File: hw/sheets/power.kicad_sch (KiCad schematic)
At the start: 36 parts, among them U1 AP62600SJ-7, U2 AP62300WU-7, U3 MCP4661-104E_ST, U4 TPS22990DMLR, U5 AZ1117CH-3.3TRG1, U6 AZ1117CH-1.8TRG1, U7 AP62300WU-7

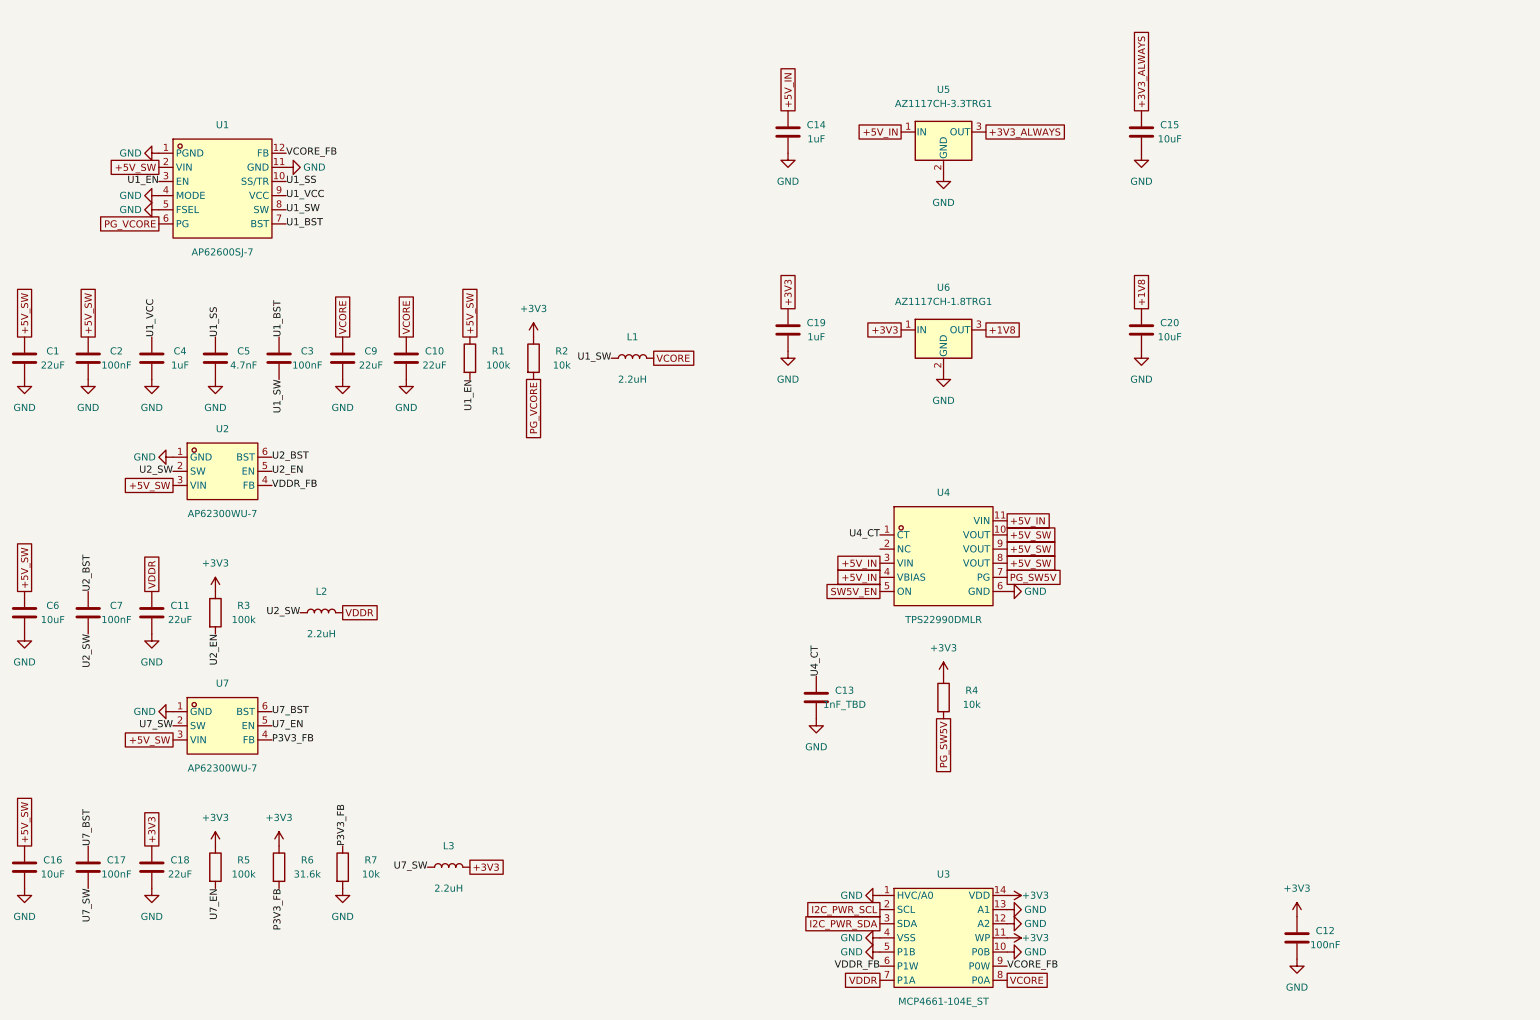
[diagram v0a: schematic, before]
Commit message: Carrier board: BMC power isolation, ESP-Hosted link, GPIO expander
Rebuilds the schematic to connectivity-by-label per BUILD.md (zero
wires/junctions) across all four sections, and adds the BMC power
architecture, connector crossings, and safety fixes worked out this
session:

- Dedicated BMC USB-C (J9), isolated 5V domains (+5V_BMC/+5V_ALT/+5V_SW),
  priority DC-jack-over-USB-C P-FET OR (Q1/Q2), 2:1 load-switch select
  (U4/U14) with a genuine ON-OFF-ON manual override (SW2)
- D1/D2 diode-OR so the BMC stays powered on ALT-only input without
  reopening the J9 backfeed path
- JP1 provisioning jumper + mandatory bring-up checklist: gates SW2 until
  the digipot's NV memory has been confirmed safe, closing the
  factory-mid-scale-default overvoltage gap on VCORE
- GPIO expander (U15, TCA9555PWR) frees 9 ESP32 GPIOs for a full-duplex
  SPI link to the interposer SoC (ESP-Hosted WiFi/BLE co-processor),
  while keeping flash chip-select and power-domain switching native for
  margin testing
- microSD, headphone jack, and both MIPI camera FFCs now cross the DDR4
  connector to the interposer, with GND isolation around each block
- J2/J3 share one USB host data pair to the interposer (peripheral use,
  independent of J2's power role)
- Added missing primary SOIC-8 NOR flash chip (W25Q32JVSS) to match the
  reference board's dual-NOR layout

docs/UNIVERSAL.md updated throughout to match; CONNECTIONS.txt and the
ESP32 pinout reference regenerated from the current netlist.
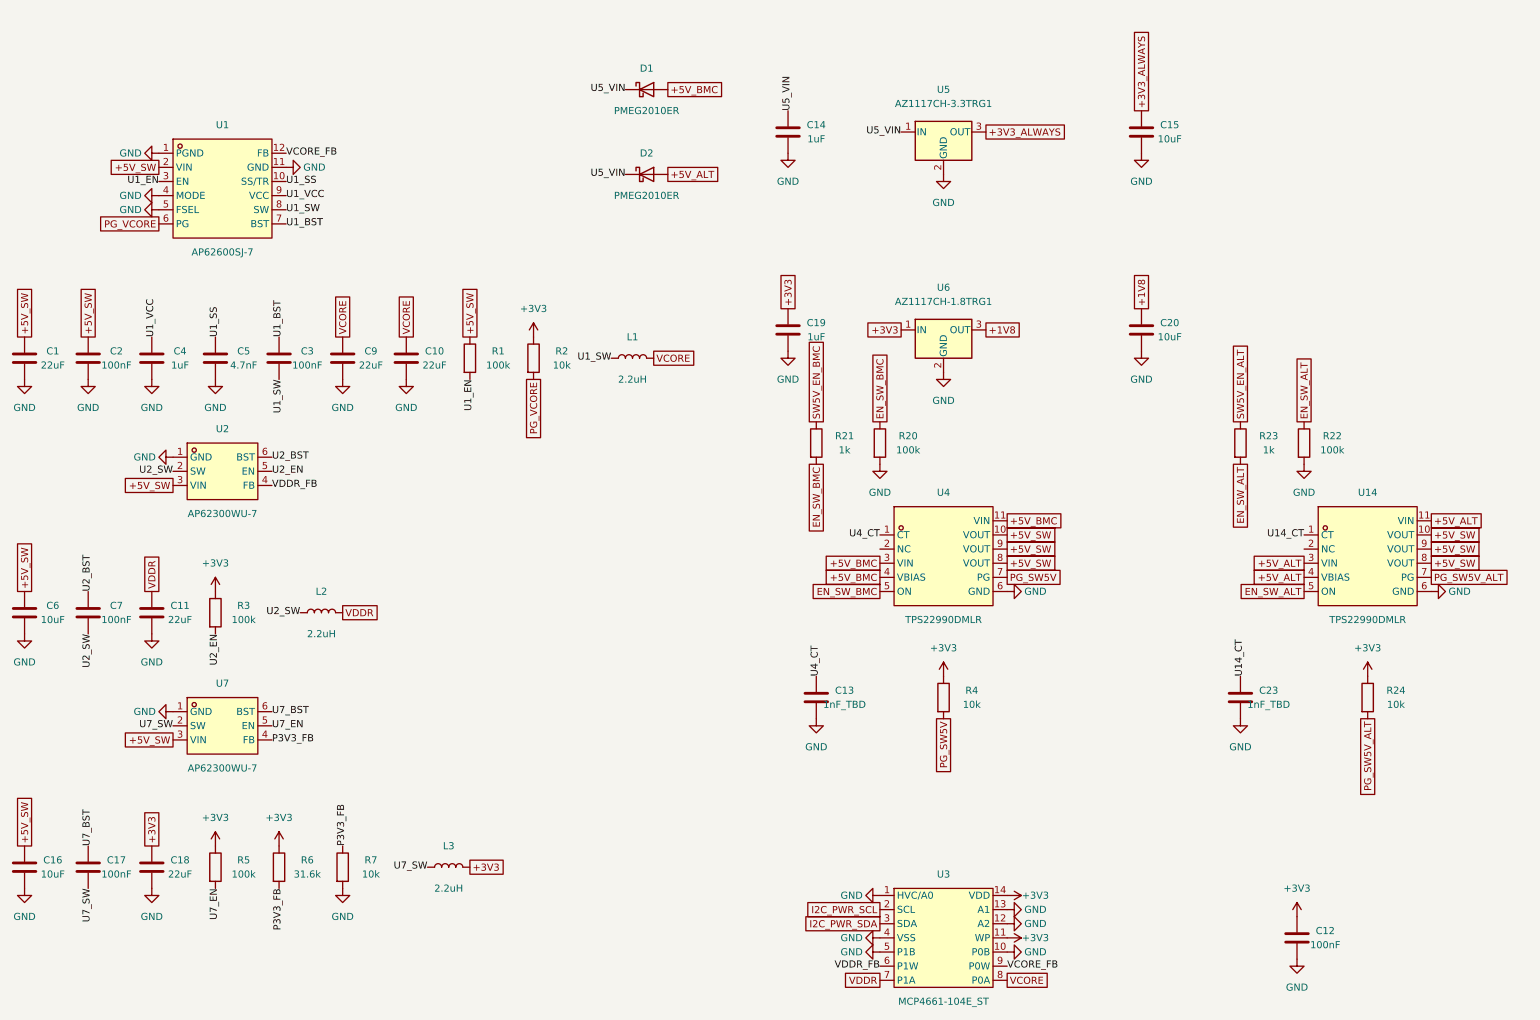
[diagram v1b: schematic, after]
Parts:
- added C23: 1nF_TBD, Capacitor_SMD:C_0402_1005Metric, symbol Device:C
- added D1, D2: PMEG2010ER, Diode_SMD:D_SOD-123W, symbol Device:D_Schottky
- added R20, R22: 100k, Resistor_SMD:R_0402_1005Metric, symbol Device:R
- added R21, R23: 1k, Resistor_SMD:R_0402_1005Metric, symbol Device:R
- added R24: 10k, Resistor_SMD:R_0402_1005Metric, symbol Device:R
- added U14: TPS22990DMLR, teacup-carrier:WSON-10_L3.0-W2.0-P0.50-BL-EP_TI_DML, symbol teacup-carrier:TPS22990DMLR
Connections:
- net +3V3: now also R24.1
- net +5V_SW: now also U14.10 (VOUT), U14.8 (VOUT), U14.9 (VOUT)
- net GND: now also C23.2, R20.2, R22.2, U14.6 (GND)
- net +5V_IN renamed +5V_BMC
- net +5V_BMC: now also D1.2 (A); no longer C14.1, U5.1 (IN)
- net SW5V_EN renamed EN_SW_BMC
- net EN_SW_BMC: now also R20.1, R21.2
- new net +5V_ALT: D2.2 (A), U14.11 (VIN), U14.3 (VIN), U14.4 (VBIAS)
- new net EN_SW_ALT: R22.1, R23.2, U14.5 (ON)
- new net PG_SW5V_ALT: R24.2, U14.7 (PG)
- new net SW5V_EN_ALT: R23.1
- new net SW5V_EN_BMC: R21.1
- new net U14_CT: C23.1, U14.1 (CT)
- new net U5_VIN: C14.1, D1.1 (K), D2.1 (K), U5.1 (IN)
